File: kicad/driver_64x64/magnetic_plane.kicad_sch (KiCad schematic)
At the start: 14 parts

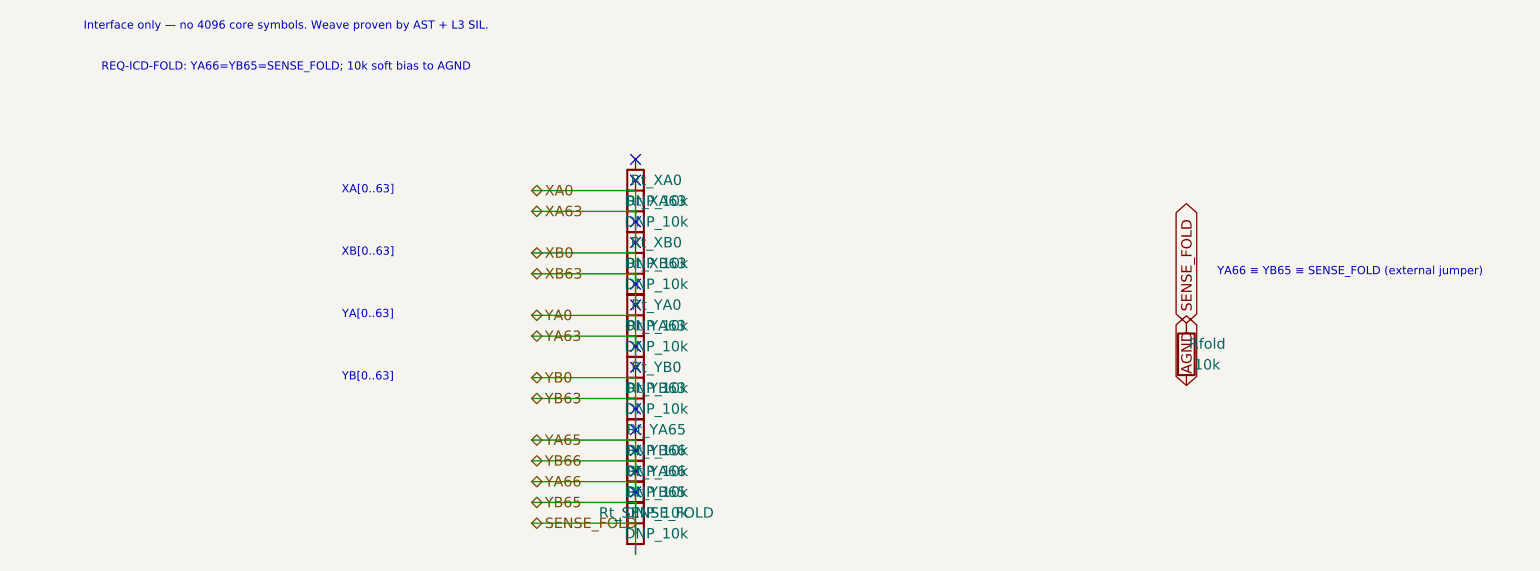
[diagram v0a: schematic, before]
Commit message: logical seperation into host and multiple decode/drive/steering boards
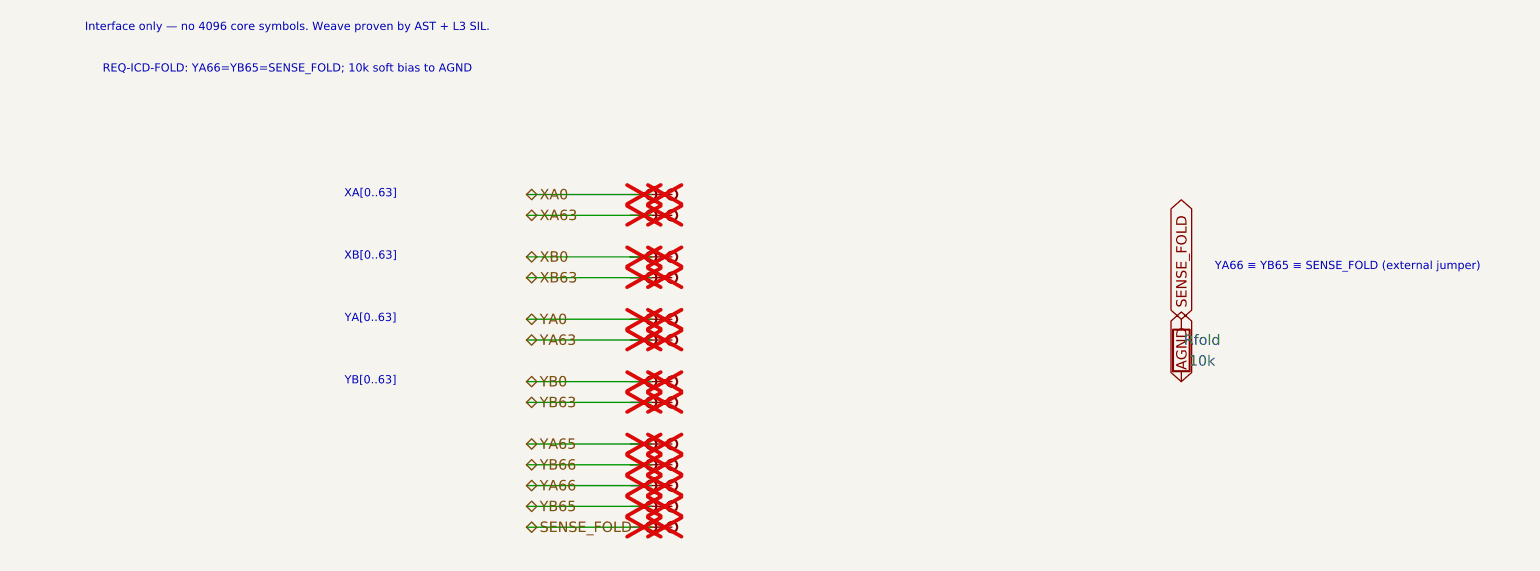
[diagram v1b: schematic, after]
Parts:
- removed Rt_SENSE_FOLD, Rt_XA0, Rt_XA63, Rt_XB0, Rt_XB63, Rt_YA0, Rt_YA63, Rt_YA65, Rt_YA66, Rt_YB0, Rt_YB63, Rt_YB65, Rt_YB66: DNP_10k, symbol Device:R
- added TP_SENSE_FOLD, TP_SENSE_FOLDb, TP_XA0, TP_XA0b, TP_XA63, TP_XA63b, TP_XB0, TP_XB0b, TP_XB63, TP_XB63b, TP_YA0, TP_YA0b, TP_YA63, TP_YA63b, TP_YA65, TP_YA65b, TP_YA66, TP_YA66b, TP_YB0, TP_YB0b, TP_YB63, TP_YB63b, TP_YB65, TP_YB65b, TP_YB66, TP_YB66b: Stub, symbol CMR:Stub
- Rfold: symbol Device:R -> CMR:R
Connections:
- net SENSE_FOLD: now also TP_SENSE_FOLD.1, TP_SENSE_FOLDb.1
- net XA0: now also TP_XA0.1, TP_XA0b.1
- net XB0: now also TP_XB0.1, TP_XB0b.1
- net YA0: now also TP_YA0.1, TP_YA0b.1
- net YB0: now also TP_YB0.1, TP_YB0b.1
- new net XA63: TP_XA63.1, TP_XA63b.1
- new net XB63: TP_XB63.1, TP_XB63b.1
- new net YA63: TP_YA63.1, TP_YA63b.1
- new net YA65: TP_YA65.1, TP_YA65b.1
- new net YA66: TP_YA66.1, TP_YA66b.1
- new net YB63: TP_YB63.1, TP_YB63b.1
- new net YB65: TP_YB65.1, TP_YB65b.1
- new net YB66: TP_YB66.1, TP_YB66b.1
- no-connect marks 13 -> 0
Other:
- moved on the sheet: Rfold
